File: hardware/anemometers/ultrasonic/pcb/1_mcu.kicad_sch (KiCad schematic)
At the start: 64 parts, among them Q1 SI2301CDS-T1-GE3, SW1 B3U-1000P, U1 TCAN330GDCNR, U2 STM32L476RGT6, U3 XC6206P332MR, X1 32.768KHz, X2 25M

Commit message: DRC clear
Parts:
- removed ?: A_A4, ProDoc_Qin-easyedapro:, symbol ProDoc_Qin-easyedapro:A_A4
- gave numbers to parts that had none: 5
- renumbered BAT to BAT1, CAN to CAN1, DEBUG to DEBUG1, I2C to I2C1, RST to RST1, SD to SD1, SPI to SPI1, SWD to SWD1, UART to UART3, USB to USB1, VBAT to VBAT1
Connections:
- net RAIN_LED: no longer names the net of U2.20 (PA4)
- no-connect marks 0 -> 8
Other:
- moved on the sheet: BAT1, C1, C10, C11, C12, C13, C14, C15, C16, C17, C18, C19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

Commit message: update
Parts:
- removed C10: 100nF, ProDoc_Qin-easyedapro:C0402, symbol ProDoc_Qin-easyedapro:100nF
- removed C11: 1uF, ProDoc_Qin-easyedapro:C0402, symbol ProDoc_Qin-easyedapro:1uF
- removed MIC1: MP34DT06JTR, ProDoc_Qin-easyedapro:MIC-SMD_5P-L3.0-W4.0-P0.85-BL, symbol ProDoc_Qin-easyedapro:MP34DT06JTR
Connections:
- net RAIN_SENS: no longer U2.15 (PA1)
- net MIC_CLK: no longer names the net of U2.10 (PC2)
- net MIC_DAT: no longer names the net of U2.8 (PC0)
- new net ADC_CH6: U13.
- no-connect marks 8 -> 11

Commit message: Latest updates!
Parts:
- DEBUG1, SWD1, UART3: now not fitted; now left out of the parts list
- U12, U13, U14, U15, U16: now left out of the parts list
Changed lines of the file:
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@@
 		(unit 1)
 		(exclude_from_sim no)
-		(in_bom yes)
+		(in_bom no)
 		(on_board yes)
 		(dnp no)
@@
 		)
 		(property "spiceSymbolName" "B5819W_C8598"
-			(at 270.51 185.42 0)
+			(at 271.526 171.958 0)
 			(effects
 				(font
@@
 		(dnp no)
 		(property "Reference" "VBAT1"
-			(at 237.49 189.1538 90)
+			(at 229.108 183.642 90)
 			(effects
 				(font
@@
 		)
 		(property "Add into BOM" "yes"
-			(at 234.95 187.96 90)
+			(at 240.03 183.388 90)
 			(effects
 				(font
@@
 		)
 		(property "Origin Footprint" "C0603"
-			(at 234.95 187.96 90)
+			(at 223.266 187.96 90)
 			(effects
 				(font
@@
 		)
 		(property "nameAlias" "Capacitance"
-			(at 234.95 187.96 90)
+			(at 223.266 187.96 90)
 			(effects
 				(font
@@
 		)
 		(property "spiceSymbolName" "CL10A475KO8NNNC"
-			(at 234.95 187.96 90)
+			(at 234.696 176.022 90)
 			(effects
 				(font
@@
 		(unit 1)
 		(exclude_from_sim no)
-		(in_bom yes)
+		(in_bom no)
 		(on_board yes)
-		(dnp no)
+		(dnp yes)
 		(property "Reference" "DEBUG1"
 			(at 321.31 54.4576 0)
@@
 		(unit 1)
 		(exclude_from_sim no)
-		(in_bom yes)
+		(in_bom no)
 		(on_board yes)
 		(dnp no)
@@
 		(unit 1)
 		(exclude_from_sim no)
-		(in_bom yes)
+		(in_bom no)
 		(on_board yes)
 		(dnp no)
@@
 		(unit 1)
 		(exclude_from_sim no)
-		(in_bom yes)
+		(in_bom no)
 		(on_board yes)
-		(dnp no)
+		(dnp yes)
 		(property "Reference" "SWD1"
 			(at 274.1168 44.2976 90)
@@
 		(unit 1)
 		(exclude_from_sim no)
-		(in_bom yes)
+		(in_bom no)
 		(on_board yes)
 		(dnp no)
@@
 		(unit 1)
 		(exclude_from_sim no)
-		(in_bom yes)
+		(in_bom no)
 		(on_board yes)
-		(dnp no)
+		(dnp yes)
 		(property "Reference" "UART3"
 			(at 291.8968 44.2976 90)
@@
 		(unit 1)
 		(exclude_from_sim no)
-		(in_bom yes)
+		(in_bom no)
 		(on_board yes)
 		(dnp no)

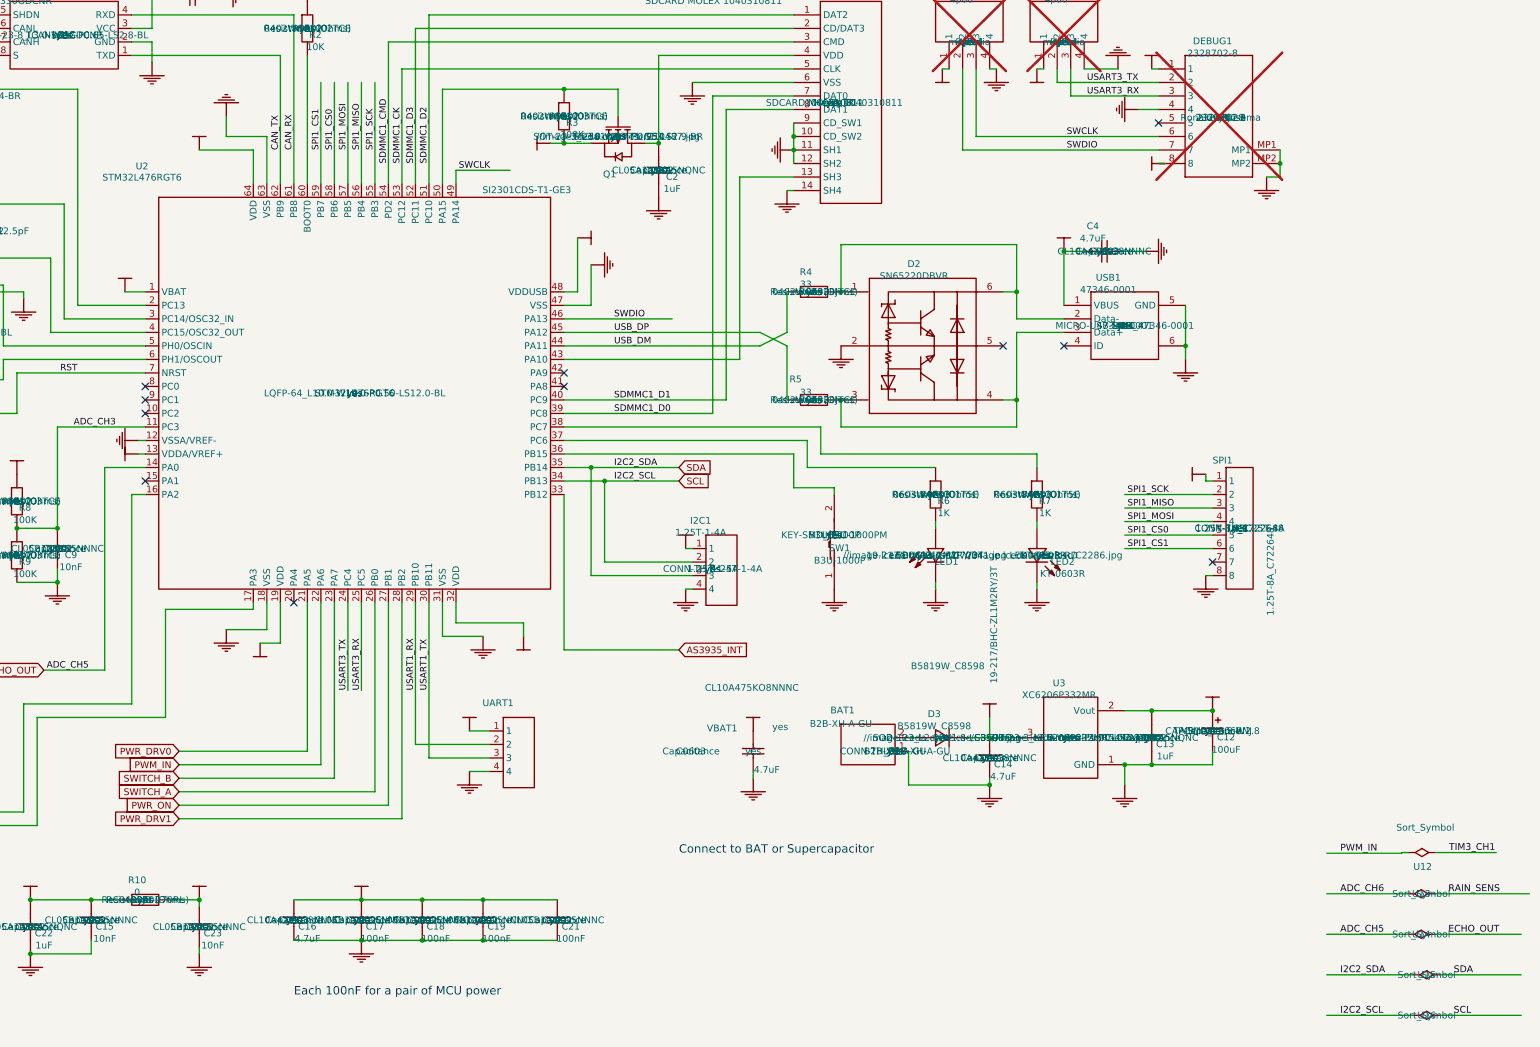
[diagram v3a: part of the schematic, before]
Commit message: Fix SD Card part number
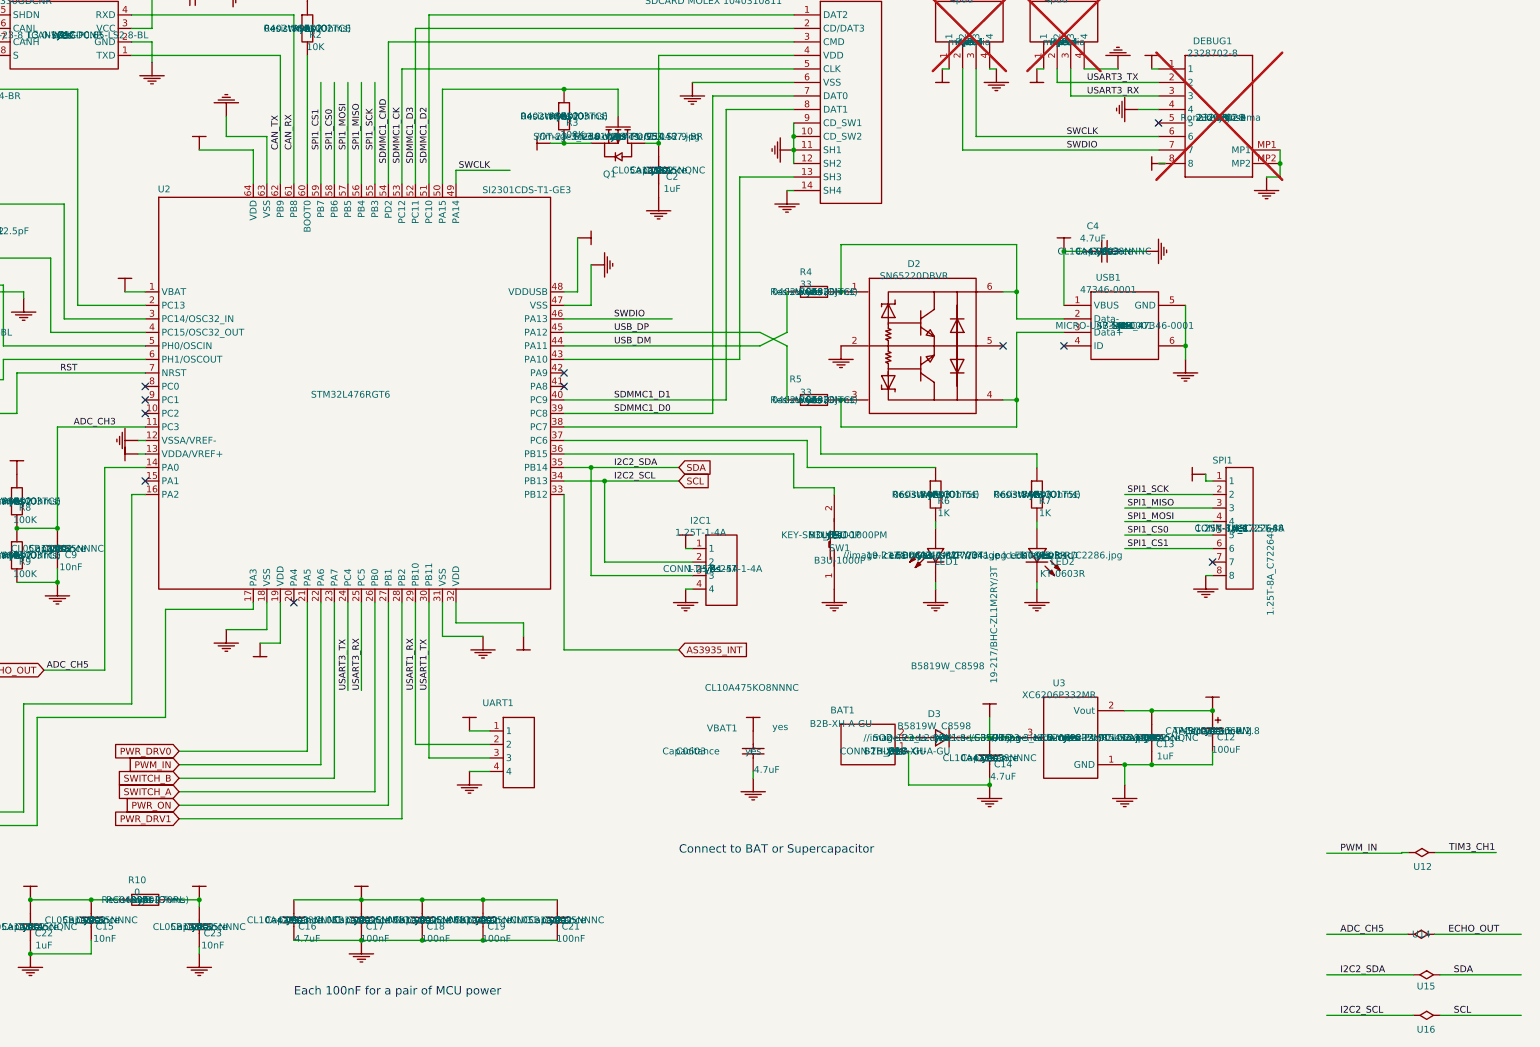
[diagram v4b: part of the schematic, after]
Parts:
- removed U13: Sort_Symbol, ProDoc_Qin-easyedapro:, symbol ProDoc_Qin-easyedapro:d8f82a34bc8fbed0
- SD1: Manufacturer (none) -> MOLEX; Manufacturer Part (none) -> 1040310811; Supplier MOLEX -> LCSC; Supplier Part 1040310811 -> C585350
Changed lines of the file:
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@@
 	(wire
 		(pts
-			(xy 363.093 214.757) (xy 380.873 214.757)
-		)
-		(stroke
-			(width 0)
-			(type default)
-		)
-	)
-	(wire
-		(pts
 			(xy 316.23 111.76) (xy 316.23 104.14)
 		)
@@
 	(wire
 		(pts
-			(xy 342.773 214.757) (xy 358.013 214.757)
-		)
-		(stroke
-			(width 0)
-			(type default)
-		)
-	)
-	(wire
-		(pts
 			(xy 120.65 134.62) (xy 113.03 134.62)
 		)
@@
 		)
 	)
-	(label "RAIN_SENS"
-		(at 365.633 214.757 0)
-		(effects
-			(font
-				(size 1.27 1.27)
-			)
-			(justify left bottom)
-		)
-	)
 	(label "USART3_TX"
 		(at 297.688 62.23 0)
@@
 		)
 	)
-	(label "ADC_CH6"
-		(at 345.313 214.757 0)
-		(effects
-			(font
-				(size 1.27 1.27)
-			)
-			(justify left bottom)
-		)
-	)
 	(label "USART2_TX"
 		(at 83.058 199.39 0)
@@
 		(dnp no)
 		(property "Reference" "U2"
-			(at 120.0404 77.978 0)
+			(at 124.206 82.296 0)
 			(effects
 				(font
@@
 		)
 		(property "Value" "STM32L476RGT6"
-			(at 120.0404 80.0862 0)
+			(at 159.258 120.904 0)
 			(effects
 				(font
@@
 					(size 1.27 1.27)
 				)
+				(hide yes)
 			)
 		)
@@
 					(size 1.27 1.27)
 				)
+				(hide yes)
 			)
 		)
@@
 					(size 1.27 1.27)
 				)
+				(hide yes)
 			)
 		)
@@
 					(size 1.27 1.27)
 				)
+				(hide yes)
 			)
 		)
@@
 					(size 1.27 1.27)
 				)
+				(hide yes)
 			)
 		)
@@
 		(dnp no)
 		(property "Reference" "U16"
-			(at 361.569 237.617 0)
+			(at 361.442 240.284 0)
 			(effects
 				(font
@@
 					(size 1.27 1.27)
 				)
+				(hide yes)
 			)
 		)
@@
 			)
 		)
-		(property "Supplier Part" "1040310811"
+		(property "Supplier Part" "C585350"
 			(at 250.19 66.04 0)
 			(effects
@@
 			)
 		)
-		(property "Supplier" "MOLEX"
+		(property "Supplier" "LCSC"
 			(at 250.19 66.04 0)
 			(effects
@@
 					(size 1.27 1.27)
 				)
+				(hide yes)
 			)
 		)
@@
 					(size 1.27 1.27)
 				)
+				(hide yes)
 			)
 		)
@@
 					(size 1.27 1.27)
 				)
+				(hide yes)
 			)
 		)
@@
 					(size 1.27 1.27)
 				)
+				(hide yes)
 			)
 		)
@@
 					(size 1.27 1.27)
 				)
+				(hide yes)
 			)
 		)
 		(property "spiceSymbolName" "SDCARD MOLEX 1040310811"
+			(at 261.366 87.122 0)
+			(effects
+				(font
+					(size 1.27 1.27)
+				)
+				(hide yes)
+			)
+		)
+		(property "Manufacturer Part" "1040310811"
 			(at 250.19 66.04 0)
 			(effects
@@
 					(size 1.27 1.27)
 				)
+				(hide yes)
+			)
+		)
+		(property "Manufacturer" "MOLEX"
+			(at 250.19 66.04 0)
+			(effects
+				(font
+					(size 1.27 1.27)
+				)
+				(hide yes)
 			)
 		)
@@
 		(dnp no)
 		(property "Reference" "U15"
-			(at 361.569 229.997 0)
+			(at 361.442 232.156 0)
 			(effects
 				(font
@@
 					(size 1.27 1.27)
 				)
+				(hide yes)
 			)
 		)
@@
 					(size 1.27 1.27)
 				)
+				(hide yes)
 			)
 		)
@@
 					(size 1.27 1.27)
 				)
+				(hide yes)
 			)
 		)
@@
 					(unit 1)
 				)
-			)
-		)
-	)
-	(symbol
-		(lib_name "d8f82a34bc8fbed0_3")
-		(lib_id "ProDoc_Qin-easyedapro:d8f82a34bc8fbed0")
-		(at 360.553 214.757 0)
-		(unit 1)
-		(exclude_from_sim no)
-		(in_bom no)
-		(on_board yes)
-		(dnp no)
-		(property "Reference" "U13"
-			(at 360.553 214.757 0)
-			(effects
-				(font
-					(size 1.27 1.27)
-				)
-			)
-		)
-		(property "Value" "Sort_Symbol"
-			(at 360.553 214.757 0)
-			(effects
-				(font
-					(size 1.27 1.27)
-				)
-			)
-		)
-		(property "Footprint" "ProDoc_Qin-easyedapro:"
-			(at 360.553 214.757 0)
-			(effects
-				(font
-					(size 1.27 1.27)
-				)
-				(hide yes)
-			)
-		)
-		(property "Datasheet" ""
-			(at 360.553 214.757 0)
-			(effects
-				(font
-					(size 1.27 1.27)
-				)
-				(hide yes)
-			)
-		)
-		(property "Description" ""
-			(at 360.553 214.757 0)
-			(effects
-				(font
-					(size 1.27 1.27)
-				)
-				(hide yes)
-			)
-		)
-		(pin ""
-		)
-		(pin ""
-		)
-		(instances
-			(project ""
-				(path "/4adc9a43-9f3a-44e1-ab61-563de3288fd4/cbb659ca-1b7c-4a31-89d0-9b7906cdfb95"
-					(reference "U?")
-					(unit 1)
-				)
-			)
-			(project ""
-				(path "/a30633bf-68dd-4888-88d6-d1ee9beba30f/d8b5ed7a-2a3a-4cba-9ce3-8a59c7975a1d"
-					(reference "U13")
-					(unit 1)
-				)

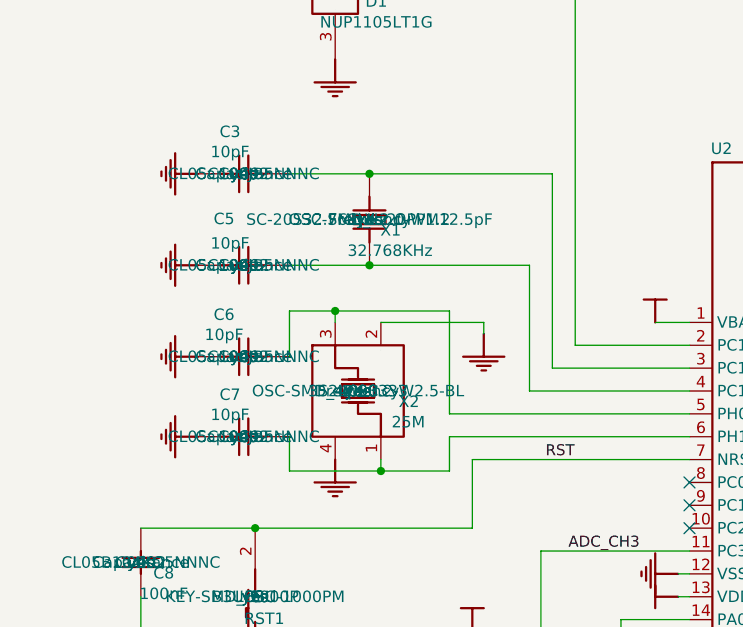
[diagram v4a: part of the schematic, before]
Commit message: Add bom
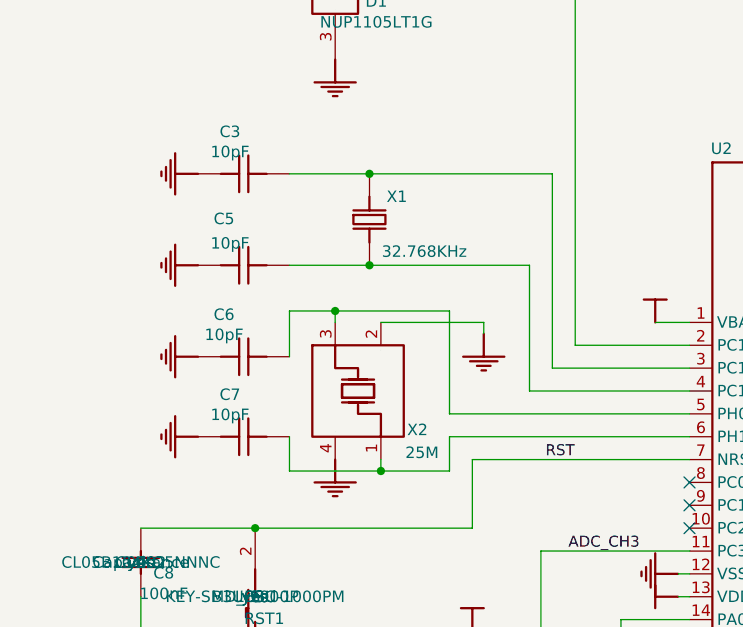
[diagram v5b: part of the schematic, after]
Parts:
- X2: Manufacturer Failong Crystal -> NDK; Manufacturer Part 3S24000333 -> NX3225GA-24MHZ-STD-CRG-2; Supplier Part C427553 -> C156248
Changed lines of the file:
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@@
 					(size 1.27 1.27)
 				)
+				(hide yes)
 			)
 		)
@@
 					(size 1.27 1.27)
 				)
+				(hide yes)
 			)
 		)
@@
 					(size 1.27 1.27)
 				)
+				(hide yes)
 			)
 		)
@@
 					(size 1.27 1.27)
 				)
+				(hide yes)
 			)
 		)
@@
 					(size 1.27 1.27)
 				)
+				(hide yes)
 			)
 		)
@@
 					(size 1.27 1.27)
 				)
+				(hide yes)
 			)
 		)
@@
 		(dnp no)
 		(property "Reference" "X2"
-			(at 89.4842 110.4138 90)
+			(at 90.424 113.538 90)
 			(effects
 				(font
@@
 		)
 		(property "Value" "25M"
-			(at 89.408 112.6744 90)
+			(at 90.932 116.078 90)
 			(effects
 				(font
@@
 			)
 		)
-		(property "Manufacturer Part" "3S24000333"
+		(property "Manufacturer Part" "NX3225GA-24MHZ-STD-CRG-2"
 			(at 83.82 109.22 0)
 			(effects
@@
 			)
 		)
-		(property "Manufacturer" "Failong Crystal"
+		(property "Manufacturer" "NDK"
 			(at 83.82 109.22 0)
 			(effects
@@
 			)
 		)
-		(property "Supplier Part" "C427553"
+		(property "Supplier Part" "C156248"
 			(at 83.82 109.22 0)
 			(effects
@@
 					(size 1.27 1.27)
 				)
+				(hide yes)
 			)
 		)
@@
 					(size 1.27 1.27)
 				)
+				(hide yes)
 			)
 		)
@@
 					(size 1.27 1.27)
 				)
+				(hide yes)
 			)
 		)
@@
 					(size 1.27 1.27)
 				)
+				(hide yes)
 			)
 		)
@@
 					(size 1.27 1.27)
 				)
+				(hide yes)
 			)
 		)
@@
 					(size 1.27 1.27)
 				)
+				(hide yes)
 			)
 		)
@@
 					(size 1.27 1.27)
 				)
+				(hide yes)
 			)
 		)
@@
 					(size 1.27 1.27)
 				)
+				(hide yes)
 			)
 		)
@@
 					(size 1.27 1.27)
 				)
+				(hide yes)
 			)
 		)
@@
 					(size 1.27 1.27)
 				)
+				(hide yes)
 			)
 		)
@@
 					(size 1.27 1.27)
 				)
+				(hide yes)
 			)
 		)
@@
 					(size 1.27 1.27)
 				)
+				(hide yes)
 			)
 		)
@@
 					(size 1.27 1.27)
 				)
+				(hide yes)
 			)
 		)
@@
 					(size 1.27 1.27)
 				)
+				(hide yes)
 			)
 		)
@@
 					(size 1.27 1.27)
 				)
+				(hide yes)
 			)
 		)
@@
 					(size 1.27 1.27)
 				)
+				(hide yes)
 			)
 		)
@@
 					(size 1.27 1.27)
 				)
+				(hide yes)
 			)
 		)
@@
 					(size 1.27 1.27)
 				)
+				(hide yes)
 			)
 		)
@@
 					(size 1.27 1.27)
 				)
+				(hide yes)
 			)
 		)
@@
 		(dnp no)
 		(property "Reference" "X1"
-			(at 87.4522 91.3638 90)
+			(at 88.138 87.63 90)
 			(effects
 				(font
@@
 		)
 		(property "Value" "32.768KHz"
-			(at 87.376 93.6244 90)
+			(at 91.186 93.726 90)
 			(effects
 				(font
@@
 					(size 1.27 1.27)
 				)
+				(hide yes)
 			)
 		)
@@
 					(size 1.27 1.27)
 				)
+				(hide yes)
 			)
 		)
@@
 					(size 1.27 1.27)
 				)
+				(hide yes)
 			)
 		)
@@
 					(size 1.27 1.27)
 				)
+				(hide yes)
 			)
 		)
@@
 					(size 1.27 1.27)
 				)
+				(hide yes)
 			)
 		)
@@
 					(size 1.27 1.27)
 				)
+				(hide yes)
 			)
 		)
@@
 					(size 1.27 1.27)
 				)
+				(hide yes)
 			)
 		)
@@
 					(size 1.27 1.27)
 				)
+				(hide yes)
 			)
 		)
@@
 					(size 1.27 1.27)
 				)
+				(hide yes)
 			)
 		)
@@
 					(size 1.27 1.27)
 				)
+				(hide yes)
 			)
 		)
@@
 					(size 1.27 1.27)
 				)
+				(hide yes)
 			)
 		)
@@
 					(size 1.27 1.27)
 				)
+				(hide yes)
 			)
 		)

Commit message: Fix mux
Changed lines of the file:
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@@
 					(size 1.27 1.27)
 				)
+				(hide yes)
 			)
 		)
@@
 					(size 1.27 1.27)
 				)
+				(hide yes)
 			)
 		)
@@
 					(size 1.27 1.27)
 				)
+				(hide yes)
 			)
 		)
@@
 					(size 1.27 1.27)
 				)
+				(hide yes)
 			)
 		)
@@
 					(size 1.27 1.27)
 				)
+				(hide yes)
 			)
 		)
@@
 					(size 1.27 1.27)
 				)
+				(hide yes)
 			)
 		)
@@
 					(size 1.27 1.27)
 				)
+				(hide yes)
 			)
 		)
@@
 					(size 1.27 1.27)
 				)
+				(hide yes)
 			)
 		)
@@
 					(size 1.27 1.27)
 				)
+				(hide yes)
 			)
 		)
@@
 					(size 1.27 1.27)
 				)
+				(hide yes)
 			)
 		)
